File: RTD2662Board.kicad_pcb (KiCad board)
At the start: 2 copper layers, 100 x 70 mm, 263 parts, among them J1 DVI, J10 UART/I2C, J11 LCD Connector, J12 SPDIFF, J13 3.5mm jack, J14 DC Jack, J15 Expansion Connector, J2 HDMI-A, J3 3.5mm jack, J4 VGA, J5 Conn_Coaxial, J6 CVBS2 In, J7 Mini-DIN-4, J8 USB B, J9 Keyboard Connector, Q1 BC846, Q2 BC846, Q3 AO3401A, Q4 BC846, Q5 AO3401A, SW1 POWER, SW2 MENU, SW3 UP, SW4 DOWN, SW5 SOURCE, U1 RTD2662, U10 W25Qxx, U11 APW7313, U12 AMS1117-1.8, U2 TPS61040DBV, U3 TSOP382xx, U4 CH341T, U5 TPS61040DBV, U6 ES7134S, U7 PAM8003, U8 TPS61040DBV, U9 AT24CS08-STUM, Y1 27MHz, Y2 12MHz

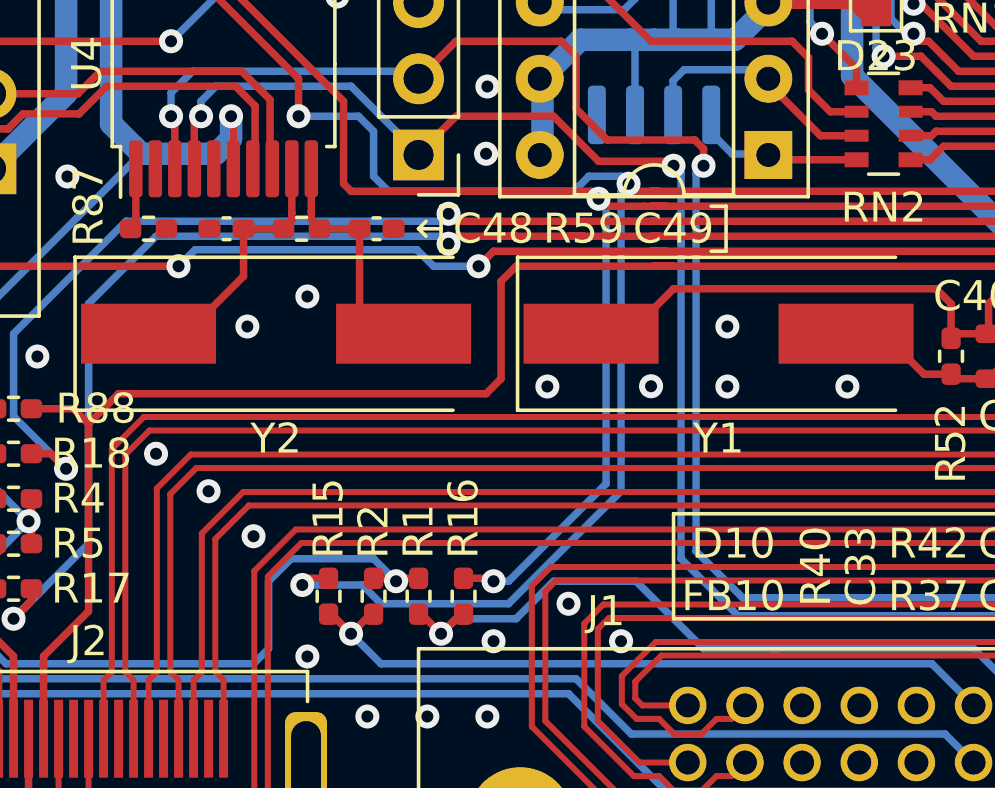
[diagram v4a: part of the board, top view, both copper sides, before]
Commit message: Changed quartz footprint to allow through hole and smd.
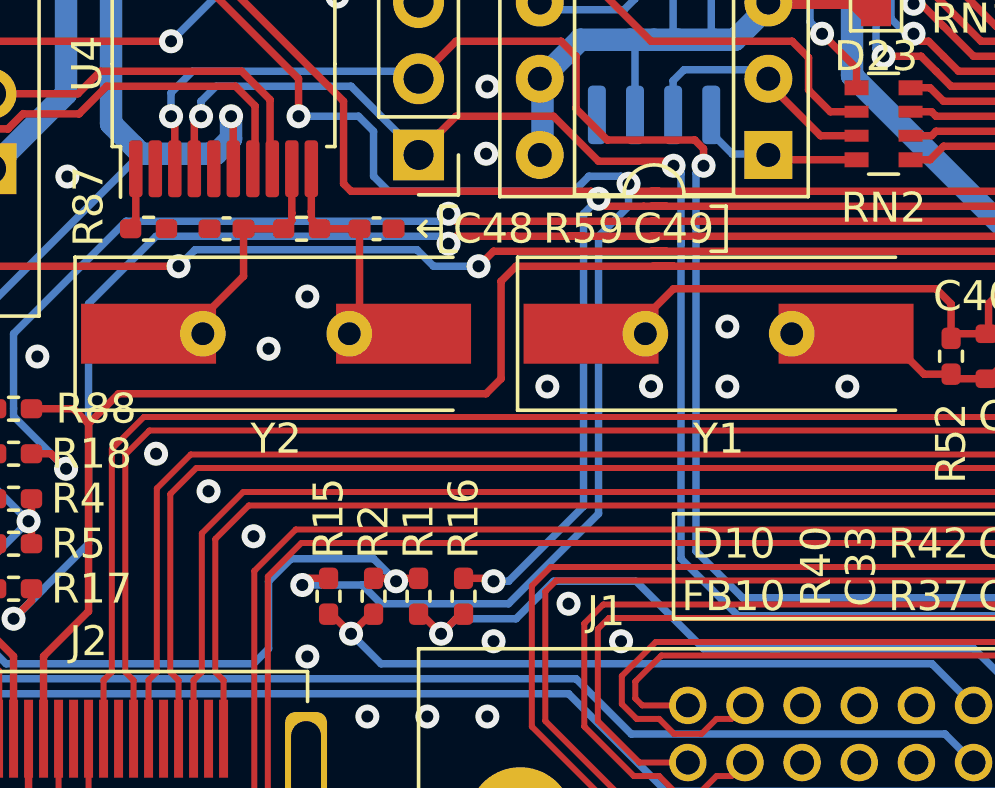
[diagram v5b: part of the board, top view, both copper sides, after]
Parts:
- D1, D10, D11, D12, D13, D14, D2, D3, D4, D5, D6, D7, D8, D9: value LXES03AAA1 -> TVS
- D23: value BAT42WS -> BAT54
- J2: value HDMI-A -> HDMI A
- J5: value Conn_Coaxial -> CVBS1
- J6: value CVBS2 In -> CVBS2
- JP3: value SolderJumper_3_Bridged12 -> LCD Power Source Select
- JP4: value SolderJumper_2_Open -> LCD Power Voltage Select
- JP5: value Common negative jumper -> Common Negative Jumper
- JP6: value Power select -> Power In Select
- L5, L6, L7: value 10uF -> 10uH
- U10: value W25Qxx -> 25x128
- U3: value TSOP382xx -> TSOP38238
- U9: value AT24CS08-STUM -> 24x01
- Y1, Y2: footprint Crystal:Crystal_SMD_HC49-SD -> RTD2662Board:Crystal_SMD_HC49-SD+HC49-U

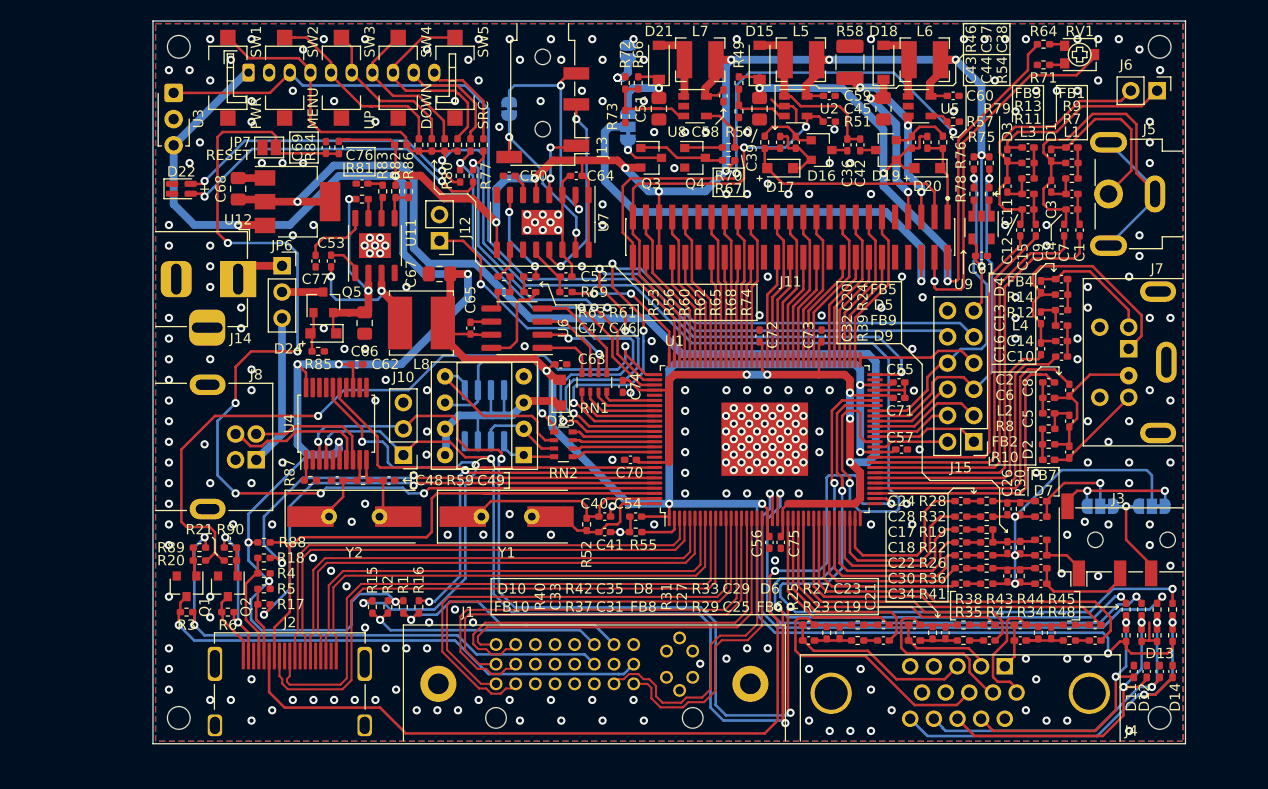
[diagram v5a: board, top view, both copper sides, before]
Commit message: Silk screen fixes
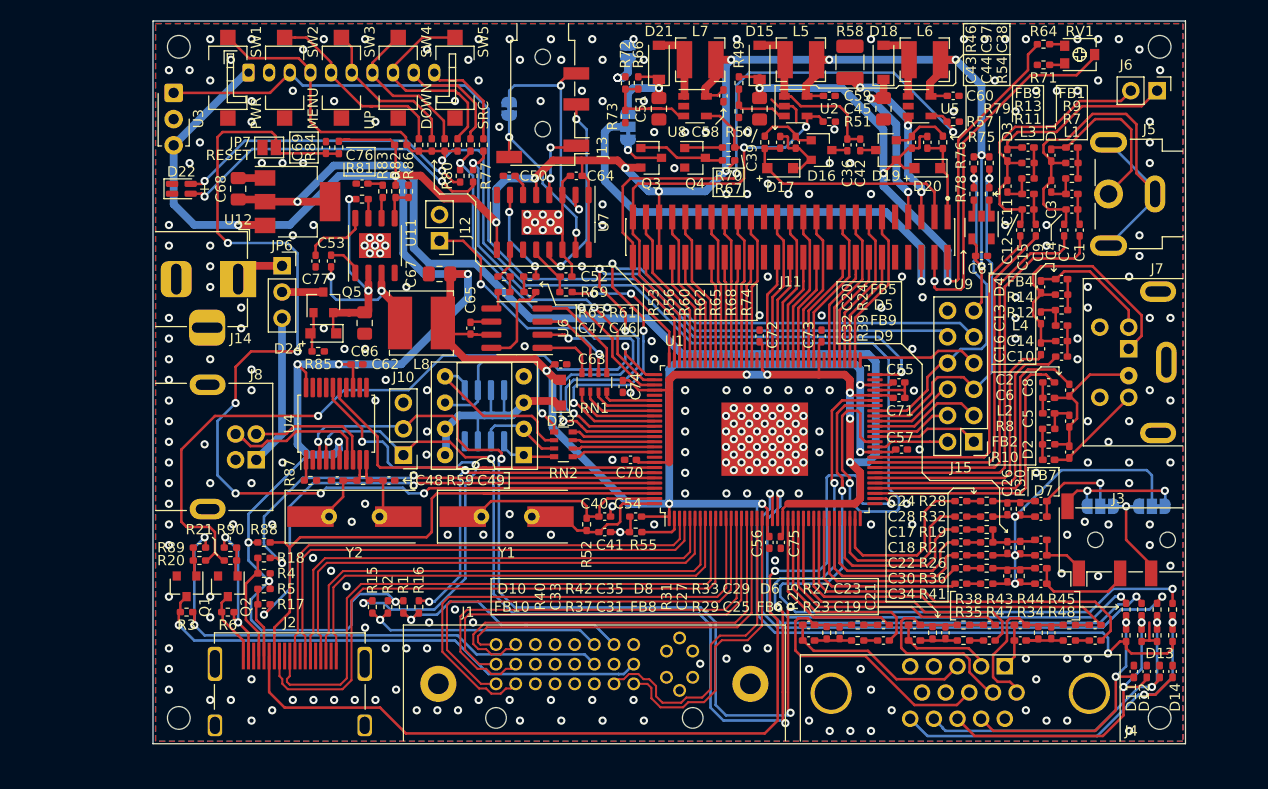
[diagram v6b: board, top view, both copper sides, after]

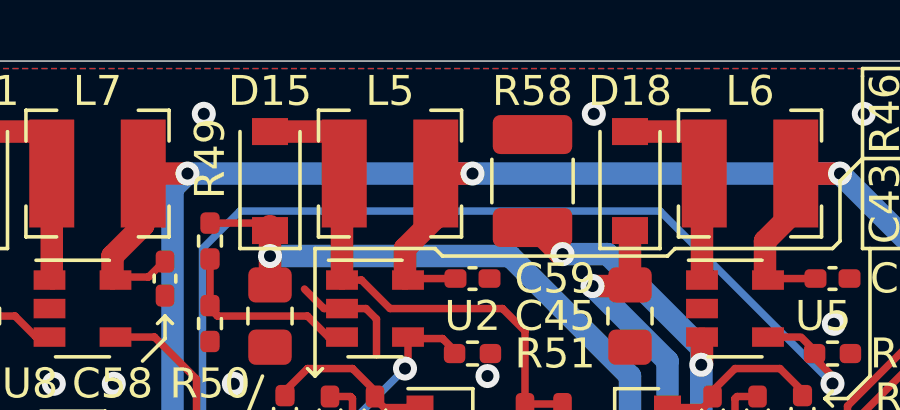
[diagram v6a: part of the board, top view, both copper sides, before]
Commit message: New adapter, fix incorrect power assignment of RTD2662 in the schematic
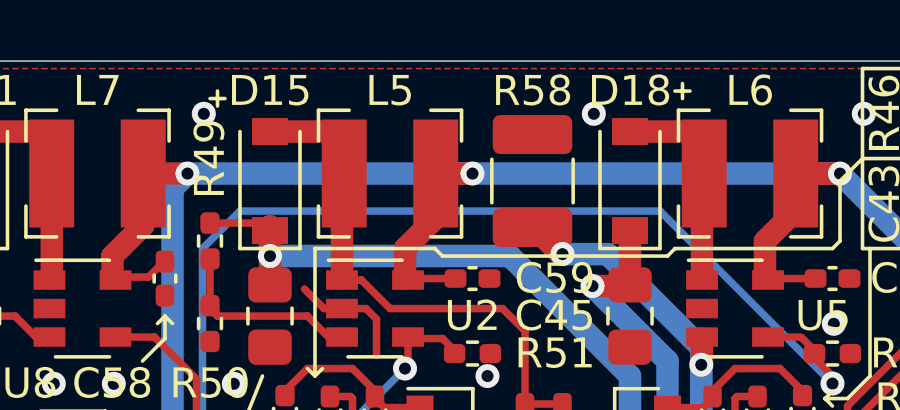
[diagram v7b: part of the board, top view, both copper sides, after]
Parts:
- L5, L6, L7, L8: value 10uH -> 6.8uH
- R24, R25, R30, R31, R39, R40: value 75 -> 75Ω
- R51, R57, R67, R70, R84, R89, R90: value 10kΩ -> 11kΩ
- R82: value 100k -> 100kΩ
- R85: value 10k -> 11kΩ
- R86: value 39k -> 39kΩ
- R88: value 47kΩ -> 27kΩ
- U3: value TSOP38238 -> TL1838
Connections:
- J1 pad 12: (no net) -> Net-(J1-Pad12)
- J1 pad 13: (no net) -> Net-(J1-Pad13)
- J1 pad 20: (no net) -> Net-(J1-Pad20)
- J1 pad 21: (no net) -> Net-(J1-Pad21)
- J1 pad 4: (no net) -> Net-(J1-Pad4)
- J1 pad 5: (no net) -> Net-(J1-Pad5)
- J1 pad 8: (no net) -> Net-(J1-Pad8)
- J1 pad C1: (no net) -> Net-(J1-PadC1)
- J1 pad C2: (no net) -> Net-(J1-PadC2)
- J1 pad C3: (no net) -> Net-(J1-PadC3)
- J1 pad C4: (no net) -> Net-(J1-PadC4)
- J11 pad 10: (no net) -> Net-(J11-Pad10)
- J11 pad 8: (no net) -> Net-(J11-Pad8)
- J11 pad 9: (no net) -> Net-(J11-Pad9)
- J4 pad 11: (no net) -> Net-(J4-Pad11)
- J4 pad 4: (no net) -> Net-(J4-Pad4)
- J4 pad 9: (no net) -> Net-(J4-Pad9)
- U1 pad 106: +1V8 -> +3V3
- U1 pad 28: (no net) -> Net-(U1-Pad28)
- U1 pad 39: (no net) -> Net-(U1-Pad39)
- U1 pad 84: +1V8 -> +3V3
- U4 pad 14: (no net) -> Net-(U4-Pad14)
- U4 pad 17: (no net) -> Net-(U4-Pad17)
- U4 pad 18: (no net) -> Net-(U4-Pad18)
- U4 pad 2: (no net) -> Net-(U4-Pad2)
- U4 pad 5: (no net) -> Net-(U4-Pad5)

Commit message: KiCad version update
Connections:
- net ~RESET~ renamed ~{RESET}
- net ~SPI_CE~ renamed ~{SPI_CE}
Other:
- net class Default removed
- net class Power removed
